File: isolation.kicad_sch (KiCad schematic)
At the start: 20 parts, among them J1201 Conn_01x02, U1201 π140U30, U1202 ISO1540, U603 XC6206P332MR

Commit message: Redo schematics
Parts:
- removed C602 (x2): 100nF, Capacitor_SMD:C_0402_1005Metric, symbol Device:C_Small
- removed R701, R702: 2k, Resistor_SMD:R_0402_1005Metric, symbol Device:R
- removed U1201: π140U30, Package_SO:SOIC-16_4.55x10.3mm_P1.27mm, symbol HALMET:pi140U30
- removed U1202: ISO1540, Package_SO:SOIC-8_3.9x4.9mm_P1.27mm, symbol Isolator:ISO1540
- added U901: π122U31, PCM_Package_SO_AKL:SOIC-8_3.9x4.9mm_P1.27mm, symbol Isolator:π122U31
- C602: footprint Capacitor_SMD:C_0402_1005Metric -> PCM_Capacitor_SMD_AKL:C_0402_1005Metric
- C605: footprint Capacitor_SMD:C_0603_1608Metric -> PCM_Capacitor_SMD_AKL:C_0603_1608Metric
- C901: renamed from C1201; footprint Capacitor_SMD:C_0402_1005Metric -> PCM_Capacitor_SMD_AKL:C_0603_1608Metric; LCSC C23733 -> C19666
- C903: renamed from C1208; footprint Capacitor_SMD:C_0402_1005Metric -> PCM_Capacitor_SMD_AKL:C_0603_1608Metric; LCSC C23733 -> C19666
- C905: renamed from C1210; footprint Capacitor_SMD:C_0402_1005Metric -> PCM_Capacitor_SMD_AKL:C_0603_1608Metric; LCSC C23733 -> C19666
- C907: renamed from C1202; footprint Capacitor_SMD:C_0402_1005Metric -> PCM_Capacitor_SMD_AKL:C_0603_1608Metric; LCSC C23733 -> C19666
- J901: renamed from J1201; value Conn_01x02 -> 3V3 Header; LCSC (none) -> C3012204
- PS901: renamed from PS1201; symbol HALMET:IB0303S-W75R3 -> HALSER:IB0303S-W75R3
- R901: renamed from R1201; footprint Resistor_SMD:R_0402_1005Metric -> PCM_Resistor_SMD_AKL:R_0402_1005Metric
- U603: footprint Package_TO_SOT_SMD:SOT-23-3 -> Package_TO_SOT_SMD:SOT-89-3; symbol HALMET:HT75xx-1-SOT23 -> HALSER:HT75xx-1-SOT23
- renumbered C1209 to C904, L1201 to L901, L1202 to L902
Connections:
- net +3.3V: now also U901.1 (VDD1)
- net +3.3V_1: now also U901.8 (VDD2)
- net GND: now also U901.4 (GND1)
- net GND1: now also U901.5 (GND2)
- net VOA: now also U901.2 (VOA)
- net iVIA: now also U901.7 (VIA)
- new net VIB: U901.3 (VIB)
- new net iVOB: U901.6 (VOB)
- no-connect marks 1 -> 0
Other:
- moved on the sheet: C602

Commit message: WIP wiring
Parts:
- C904: footprint HALMET:C_1808_4520Metric -> HALSER:C_1808_4520Metric
- U603: footprint Package_TO_SOT_SMD:SOT-89-3 -> PCM_Package_TO_SOT_SMD_AKL:SOT-23
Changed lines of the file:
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@@
+			)
+		)
+		(property "Note" ""
+			(at 123.19 60.96 0)
+			(effects
+				(font
+					(size 1.27 1.27)
+				)
+				(hide yes)
 			)
 		)
@@
 		)
 		(property "Sim.Pins" ""
+			(at 128.27 95.25 0)
+			(effects
+				(font
+					(size 1.27 1.27)
+				)
+				(hide yes)
+			)
+		)
+		(property "Note" ""
 			(at 128.27 95.25 0)
 			(effects
@@
 			)
 		)
+		(property "Note" ""
+			(at 74.93 95.25 0)
+			(effects
+				(font
+					(size 1.27 1.27)
+				)
+				(hide yes)
+			)
+		)
 		(pin "1"
 		)
@@
 			)
 		)
+		(property "Note" ""
+			(at 190.5 64.77 0)
+			(effects
+				(font
+					(size 1.27 1.27)
+				)
+				(hide yes)
+			)
+		)
 		(pin "1"
 		)
@@
 			)
 		)
+		(property "Note" ""
+			(at 69.85 63.5 0)
+			(effects
+				(font
+					(size 1.27 1.27)
+				)
+				(hide yes)
+			)
+		)
 		(pin "1"
 		)
@@
 			)
 		)
+		(property "Note" ""
+			(at 83.82 63.5 0)
+			(effects
+				(font
+					(size 1.27 1.27)
+				)
+				(hide yes)
+			)
+		)
 		(pin "1"
 		)
@@
 			)
 		)
-		(property "Footprint" "Package_TO_SOT_SMD:SOT-89-3"
+		(property "Footprint" "PCM_Package_TO_SOT_SMD_AKL:SOT-23"
 			(at 151.13 55.245 0)
 			(effects
@@
 		)
 		(property "Sim.Pins" ""
+			(at 151.13 63.5 0)
+			(effects
+				(font
+					(size 1.27 1.27)
+				)
+				(hide yes)
+			)
+		)
+		(property "Note" ""
 			(at 151.13 63.5 0)
 			(effects
@@
 			)
 		)
+		(property "Note" ""
+			(at 177.8 99.06 0)
+			(effects
+				(font
+					(size 1.27 1.27)
+				)
+				(hide yes)
+			)
+		)
 		(pin "1"
 		)
@@
 			)
 		)
+		(property "Note" ""
+			(at 101.6 63.5 0)
+			(effects
+				(font
+					(size 1.27 1.27)
+				)
+				(hide yes)
+			)
+		)
 		(pin "1"
 		)
@@
 		)
 		(property "Sim.Pins" ""
+			(at 167.64 64.77 0)
+			(effects
+				(font
+					(size 1.27 1.27)
+				)
+				(hide yes)
+			)
+		)
+		(property "Note" ""
 			(at 167.64 64.77 0)
 			(effects
@@
 			)
 		)
+		(property "Note" ""
+			(at 132.08 63.5 0)
+			(effects
+				(font
+					(size 1.27 1.27)
+				)
+				(hide yes)
+			)
+		)
 		(pin "1"
 		)
@@
 			)
 		)
+		(property "Note" ""
+			(at 77.47 60.96 0)
+			(effects
+				(font
+					(size 1.27 1.27)
+				)
+				(hide yes)
+			)
+		)
 		(pin "1"
 		)
@@
 			)
 		)
+		(property "Note" ""
+			(at 118.11 63.5 0)
+			(effects
+				(font
+					(size 1.27 1.27)
+				)
+				(hide yes)
+			)
+		)
 		(pin "1"
 		)
@@
 			)
 		)
-		(property "Footprint" "HALMET:C_1808_4520Metric"
+		(property "Footprint" "HALSER:C_1808_4520Metric"
 			(at 101.6 72.39 0)
 			(effects
@@
 		)
 		(property "Sim.Pins" ""
+			(at 101.6 72.39 0)
+			(effects
+				(font
+					(size 1.27 1.27)
+				)
+				(hide yes)
+			)
+		)
+		(property "Note" ""
 			(at 101.6 72.39 0)
 			(effects
@@
 			(at 101.6 106.68 0)
 			(effects
+				(font
+					(size 1.27 1.27)
+				)
+				(hide yes)
+			)
+		)
+		(property "Note" ""
+			(at 101.6 106.68 0)
+			(effects

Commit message: Further design adjustments
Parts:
- removed J901: 3V3 Header, Connector_PinHeader_2.54mm:PinHeader_1x02_P2.54mm_Vertical, symbol Connector_Generic:Conn_01x02

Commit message: Further manufacturing tweaks
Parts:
- C904: value 220pF/2kV -> 1nF/X1,Y2; LCSC C2940747 -> C784081
- PS901: JLCPCB_CORRECTION (none) -> 0;3.81;270
- U901: JLCPCB_CORRECTION (none) -> 0;0;270
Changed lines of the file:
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@@
+			)
+		)
+		(property "JLCPCB_CORRECTION" "0;3.81;270"
+			(at 101.6 63.5 0)
+			(effects
+				(font
+					(size 1.27 1.27)
+				)
+				(hide yes)
 			)
 		)
@@
 			)
 		)
-		(property "Value" "220pF/2kV"
+		(property "Value" "1nF/X1,Y2"
 			(at 101.6063 76.2 90)
 			(effects
@@
 			)
 		)
-		(property "LCSC" "C2940747"
+		(property "LCSC" "C784081"
 			(at 101.6 72.39 0)
 			(effects
@@
 			(at 101.6 106.68 0)
 			(effects
+				(font
+					(size 1.27 1.27)
+				)
+				(hide yes)
+			)
+		)
+		(property "JLCPCB_CORRECTION" "0;0;270"
+			(at 101.6 106.68 0)
+			(effects

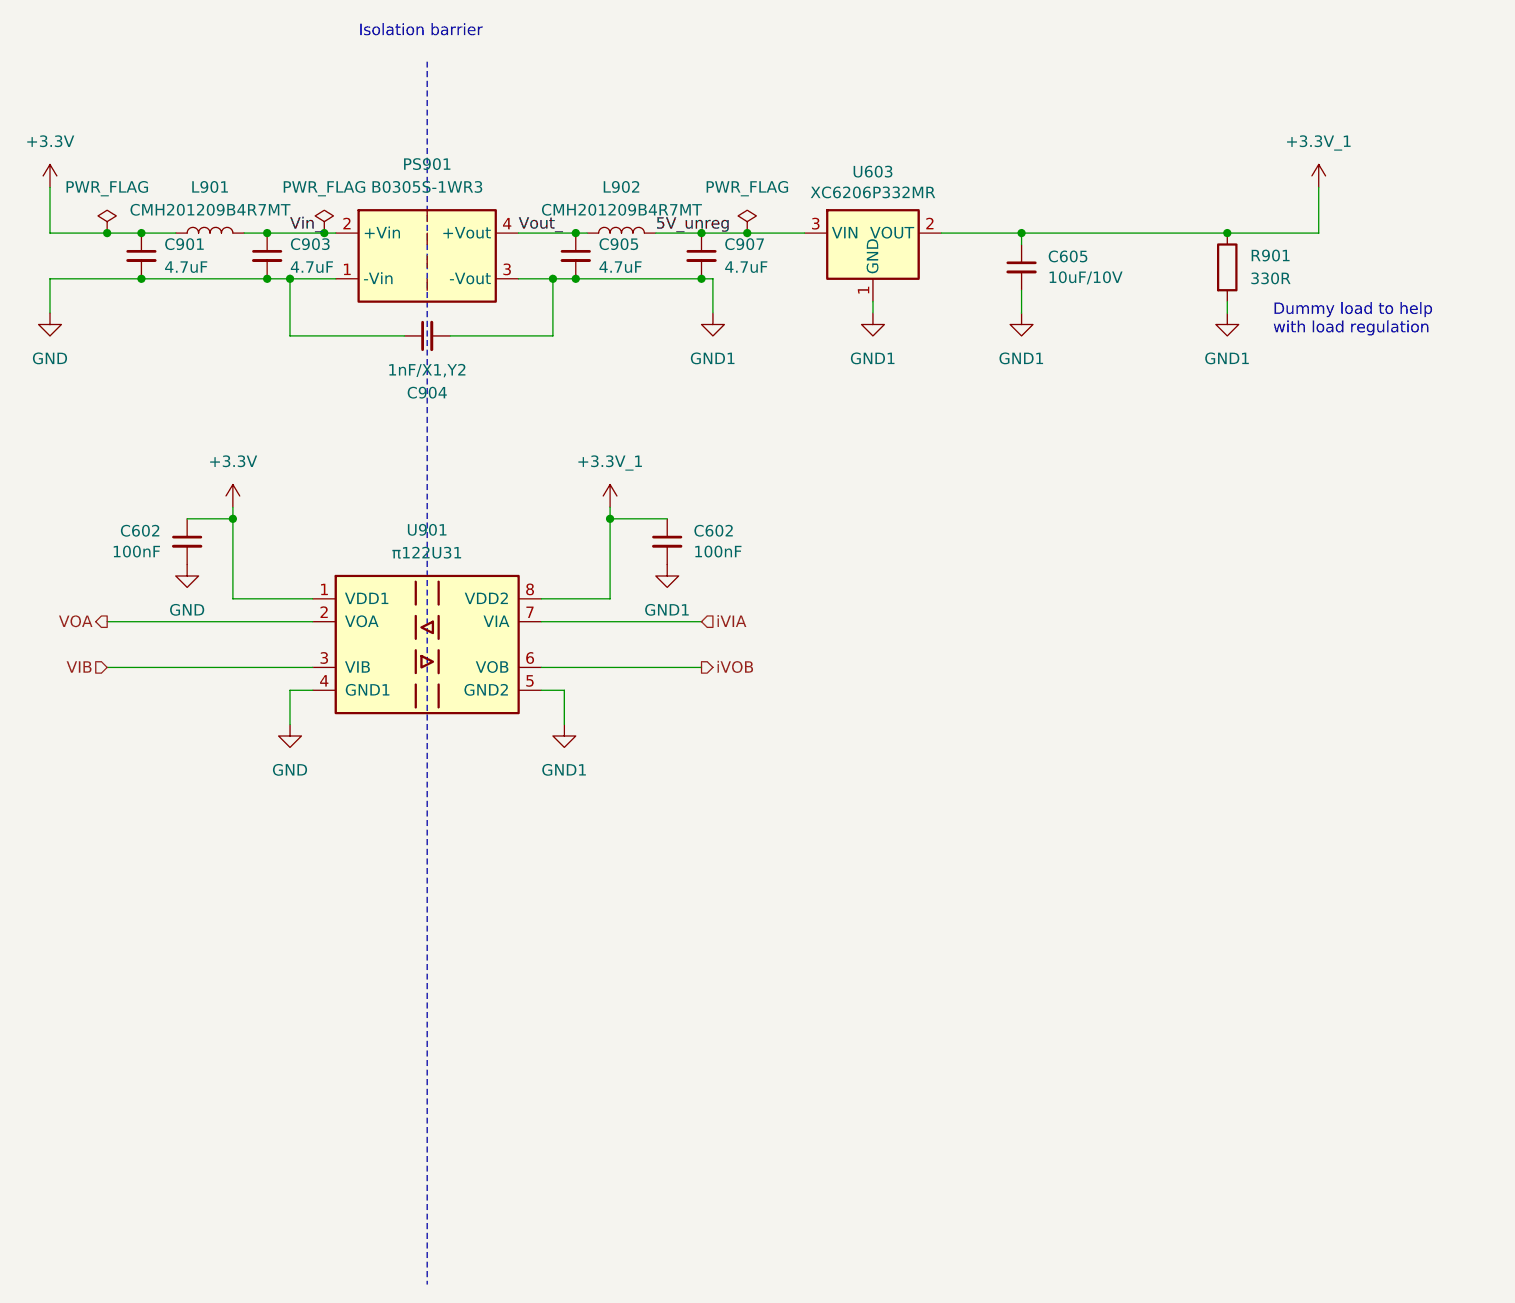
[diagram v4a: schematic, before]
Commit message: Fix issues found in -a1
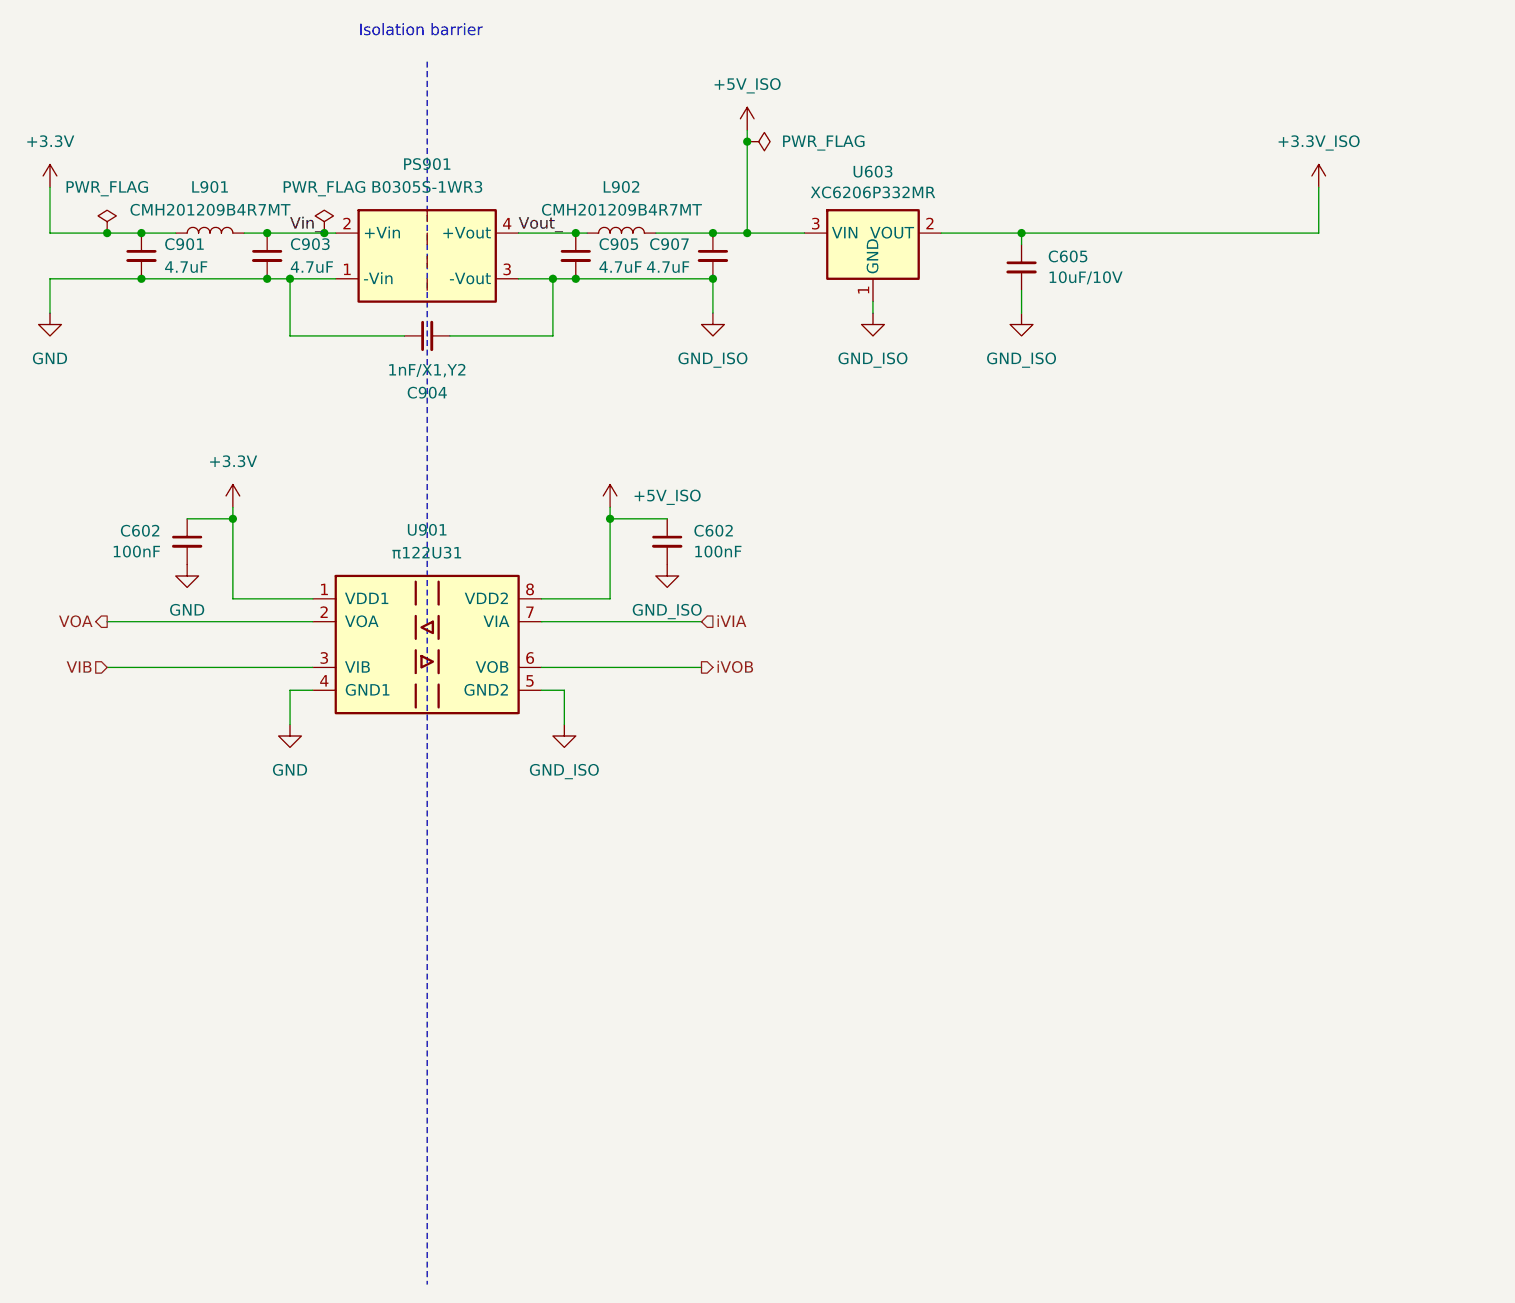
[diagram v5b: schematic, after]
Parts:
- removed R901: 330R, PCM_Resistor_SMD_AKL:R_0402_1005Metric, symbol Device:R
- C602: footprint PCM_Capacitor_SMD_AKL:C_0402_1005Metric -> Capacitor_SMD:C_0402_1005Metric
- C605, C901, C903, C905, C907: footprint PCM_Capacitor_SMD_AKL:C_0603_1608Metric -> Capacitor_SMD:C_0603_1608Metric
- U901: footprint PCM_Package_SO_AKL:SOIC-8_3.9x4.9mm_P1.27mm -> Package_SO:SOIC-8_3.9x4.9mm_P1.27mm
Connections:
- net +3.3V_1 renamed +3.3V_ISO
- net +3.3V_ISO: no longer C602.1, U901.8 (VDD2)
- net 5V_unreg renamed +5V_ISO
- net +5V_ISO: now also C602.1, U901.8 (VDD2)
- net GND1 renamed GND_ISO
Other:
- note removed: "Dummy load to help with load regulation"
- company: Hat Labs Ltd -> Hat Labs oy
- title: Hat Labs Marine Engine & Tank interface (HALMET) -> Hat Labs Serial Interface Device (HALSER)
- moved on the sheet: C907
